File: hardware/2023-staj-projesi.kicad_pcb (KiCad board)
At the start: 2 copper layers, 111.8 x 99.1 mm, 87 parts, among them J1 POWER, J2 SENSOR, J3 RELAY, J4 SW, J5 USB_B_Mini, J6 EXT, K1 SRD-05VDC-SL-C, Q1 BC847, SW1 BTN_ACT, SW2 BTN_DEACT, T1 PA2748NL, U1 LM2596S-5, U2 LM2596S-ADJ, U3 LM2596S-3.3, U4 STM32F103C8T6, U5 SIM800L-CORE, U6 AD8603, Y1 32KHz, Y2 8MHz

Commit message: PCB 5V power placed
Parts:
- moved C3 273.1 mm to (114.3, 124.5), turned to 90 degrees
- moved C6 268.0 mm to (116.8, 134.6)
- moved C12 257.5 mm to (142.2, 119.4)
- moved C9 253.6 mm to (134.6, 119.4), turned to 180 degrees
- moved D4 251.6 mm to (127.0, 134.6)
- moved U1 246.8 mm to (126.2, 119.3), turned to 90 degrees
- moved L1 222.2 mm to (139.7, 129.5)
- moved Brd1 185.5 mm to (175.5, 132.3), turned to 90 degrees
- moved C2 1.02 mm to (96.3, 119.4)

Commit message: 3.3 and 3.8 volts placed on the pcb
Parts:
- moved C8 310.7 mm to (66.0, 96.5), turned to 90 degrees
- moved C5 303.7 mm to (71.1, 107.6), turned to 90 degrees
- moved C4 291.3 mm to (88.0, 114.3)
- moved C13 286.3 mm to (99.2, 78.7)
- moved U3 283.0 mm to (75.3, 93.7), turned to 180 degrees
- moved C7 281.9 mm to (97.6, 114.3)
- moved U4 281.8 mm to (115.5, 84.7)
- moved C11 281.7 mm to (100.0, 86.4)
- moved D6 276.7 mm to (91.4, 94.0), turned to 90 degrees
- moved U2 253.3 mm to (111.8, 110.1)
- moved C10 251.4 mm to (133.0, 104.1)
- moved R3 250.4 mm to (138.0, 104.1)
- moved R2 250.4 mm to (138.0, 101.6)
- moved C14 248.5 mm to (139.5, 96.5)
- moved J5 247.0 mm to (160.7, 42.8)
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
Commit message: PCB design completed
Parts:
- added C10: 100nF/20V, Capacitor_SMD:C_0805_2012Metric, F.Cu at (159.2, 81.6)
- added C14: 100uF/20V, Capacitor_SMD:CP_Elec_6.3x7.7, F.Cu at (154.4, 83.2)
- added C4: 100uF/63V, Capacitor_SMD:CP_Elec_10x10.5, F.Cu at (161.2, 108.9)
- added C7: 470nF/100V, Capacitor_SMD:C_1206_3216Metric, F.Cu at (166.9, 99.9)
- added D5: SK56, Diode_SMD:D_SMC, F.Cu at (169.5, 95.0)
- added L2: 74477020, 2023Staj:IND_1280-WE-PD_WRE, F.Cu at (166.8, 84.6)
- added R2: 2K2, Resistor_SMD:R_0603_1608Metric, F.Cu at (151.4, 89.3)
- added R3: 1K, Resistor_SMD:R_0603_1608Metric, F.Cu at (155.2, 89.3)
- added U2: LM2596S-ADJ, Package_TO_SOT_SMD:TO-263-5_TabPin3, F.Cu at (153.9, 97.1)
- moved D10 340.7 mm to (74.9, 59.0), turned to -90 degrees
- moved U6 339.4 mm to (81.5, 60.0), turned to -90 degrees
- moved C30 339.1 mm to (77.1, 59.4), turned to -90 degrees
- moved R13 338.0 mm to (78.8, 59.4), turned to -90 degrees
- moved R14 337.9 mm to (78.8, 62.6), turned to -90 degrees
- moved C31 334.5 mm to (81.7, 63.1), turned to 180 degrees
- moved SW1 328.7 mm to (88.8, 55.1)
- moved J2 323.0 mm to (70.8, 53.9), turned to -90 degrees
- moved J3 322.9 mm to (70.8, 72.9), turned to -90 degrees
- moved D7 321.0 mm to (90.1, 48.2), turned to 90 degrees
- moved SW2 320.5 mm to (96.9, 55.1)
- moved K1 316.6 mm to (84.1, 78.0), turned to 180 degrees
- moved R7 314.4 mm to (86.8, 60.6), turned to 90 degrees
- moved D8 314.0 mm to (96.7, 48.2), turned to 90 degrees
- moved R6 311.3 mm to (90.2, 60.6), turned to 90 degrees
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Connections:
- C10 pad 2: Net-(D5-A) -> GND
- C11 pad 2: Net-(D6-A) -> GND
- C12 pad 2: Net-(D4-A) -> GND
- C13 pad 2: Net-(D6-A) -> GND
- C3 pad 2: Net-(D4-A) -> GND
- C4 pad 2: Net-(D5-A) -> GND
- C5 pad 2: Net-(D6-A) -> GND
- C6 pad 2: Net-(D4-A) -> GND
- C7 pad 2: Net-(D5-A) -> GND
- C8 pad 2: Net-(D6-A) -> GND
- C9 pad 2: Net-(D4-A) -> GND
- D4 pad 2: Net-(D4-A) -> GND
- D5 pad 2: Net-(D5-A) -> GND
- D6 pad 2: Net-(D6-A) -> GND
- J6 pad 10: /MCU/I2C2_SCL -> /MCU/I2C2_SDA
- J6 pad 12: /MCU/I2C2_SDA -> /MCU/I2C2_SCL
- R3 pad 2: Net-(D5-A) -> GND
- U1 pad 3: Net-(D4-A) -> GND
- U1 pad 5: Net-(D4-A) -> GND
- U2 pad 3: Net-(D5-A) -> GND
- U2 pad 5: Net-(D5-A) -> GND
- U3 pad 3: Net-(D6-A) -> GND
- U3 pad 5: Net-(D6-A) -> GND
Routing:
- net /Power/+12V: track 0.00 -> 378.2 mm, vias 0 -> 4
- net +3V3: track 0.00 -> 349.0 mm, vias 0 -> 7
- net +5V: track 0.00 -> 329.8 mm, vias 0 -> 1
- net +3V8: track 0.00 -> 141.8 mm
- net /MCU/USB_D+: track 0.00 -> 96.3 mm, vias 0 -> 2
- net /MCU/LED_ACT: track 0.00 -> 96.2 mm, vias 0 -> 2
- net /MCU/USB_D-: track 0.00 -> 96.1 mm, vias 0 -> 2
- net /MCU/LED_DEACT: track 0.00 -> 88.9 mm, vias 0 -> 2
- net /MCU/LED_ERR: track 0.00 -> 82.1 mm, vias 0 -> 2
- net /MCU/BTN_ACT: track 0.00 -> 62.0 mm, vias 0 -> 2
- net /GSM/RXD: track 0.00 -> 60.4 mm
- net /ADC/ADC: track 0.00 -> 59.8 mm, vias 0 -> 2
- net /MCU/I2C2_SCL: track 0.00 -> 59.4 mm, vias 0 -> 2
- net /MCU/BTN_DEACT: track 0.00 -> 59.3 mm, vias 0 -> 2
- net /GSM/TXD: track 0.00 -> 58.7 mm
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- added copper zone on F.Cu, net GND
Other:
- board text added: "2023 STAJ PROJESI"
- board text added: "Lorem ipsum dolor sit amet consectetur adipiscing elit, urna consequat felis vehicula class ultricies mollis dictumst, aenean non a in donec nulla. Phasellus ante pellentesque erat cum risus consequat imperdiet aliquam, integer placerat et turpis mi eros nec lobortis taciti, vehicula nisl litora tellus ligula porttitor metus."

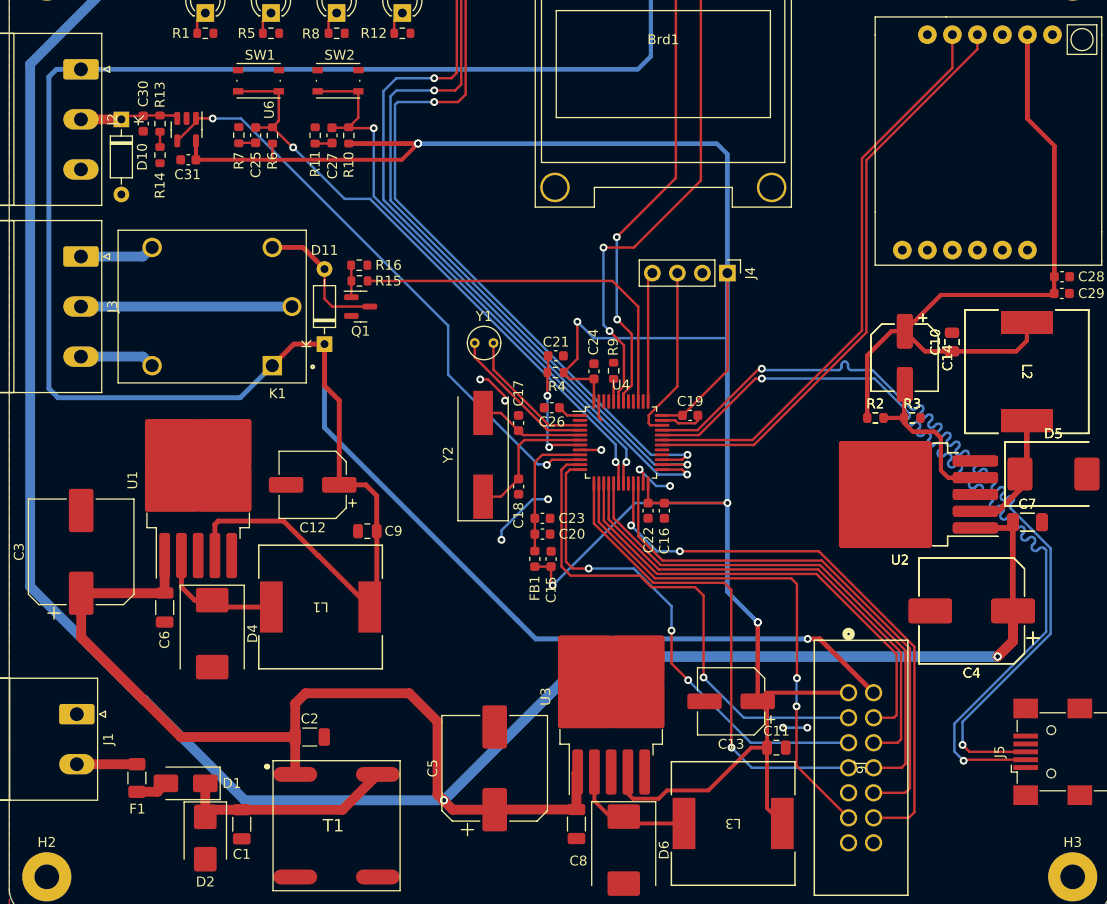
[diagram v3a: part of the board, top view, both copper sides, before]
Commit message: Added PCB names and logos
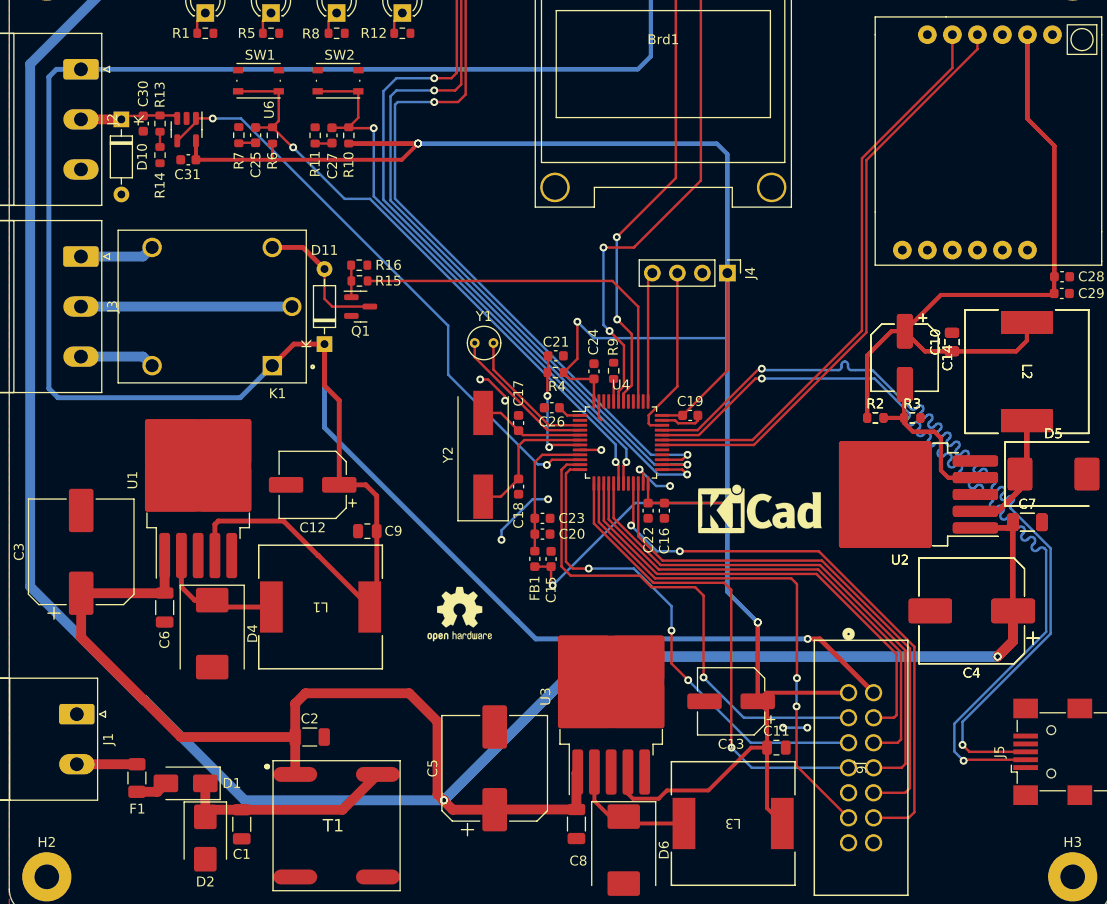
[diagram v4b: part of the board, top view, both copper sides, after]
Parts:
- added REF**: KiCad-Logo_5mm_SilkScreen, Symbol:KiCad-Logo_5mm_SilkScreen, F.Cu at (139.7, 99.1)
- added REF**: OSHW-Logo2_7.3x6mm_SilkScreen, Symbol:OSHW-Logo2_7.3x6mm_SilkScreen, F.Cu at (109.2, 109.2)
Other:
- board text added: "2023 INTERSHIP PROJECT HIDRO ELEKTRONIK"
- board text added: "Asli VEZIR Yilmaz Can DURAN Mehmet Emre SAYGI"
- board text removed: "2023 STAJ PROJESI"
- board text removed: "Lorem ipsum dolor sit amet consectetur adipiscing elit, urna consequat felis vehicula class ultricies mollis dictumst, aenean non a in donec nulla. Phasellus ante pellentesque erat cum risus consequat imperdiet aliquam, integer placerat et turpis mi eros nec lobortis taciti, vehicula nisl litora tellus ligula porttitor metus."
